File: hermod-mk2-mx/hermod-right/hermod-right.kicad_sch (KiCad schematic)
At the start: 45 parts, among them J1 USB_C_Receptacle_USB2.0, J2 Conn_01x05, J3 USB_C_Receptacle_USB2.0, Q3 MMUN2133LT1G, U1 STM32G474CETx, U2 PRTR5V0U2X, U3 XC6206PxxxMR-Regulator_Linear, U4 CR2013-MI2120, U5 PRTR5V0U2X, U8 SN74AHCT1G125DBVR

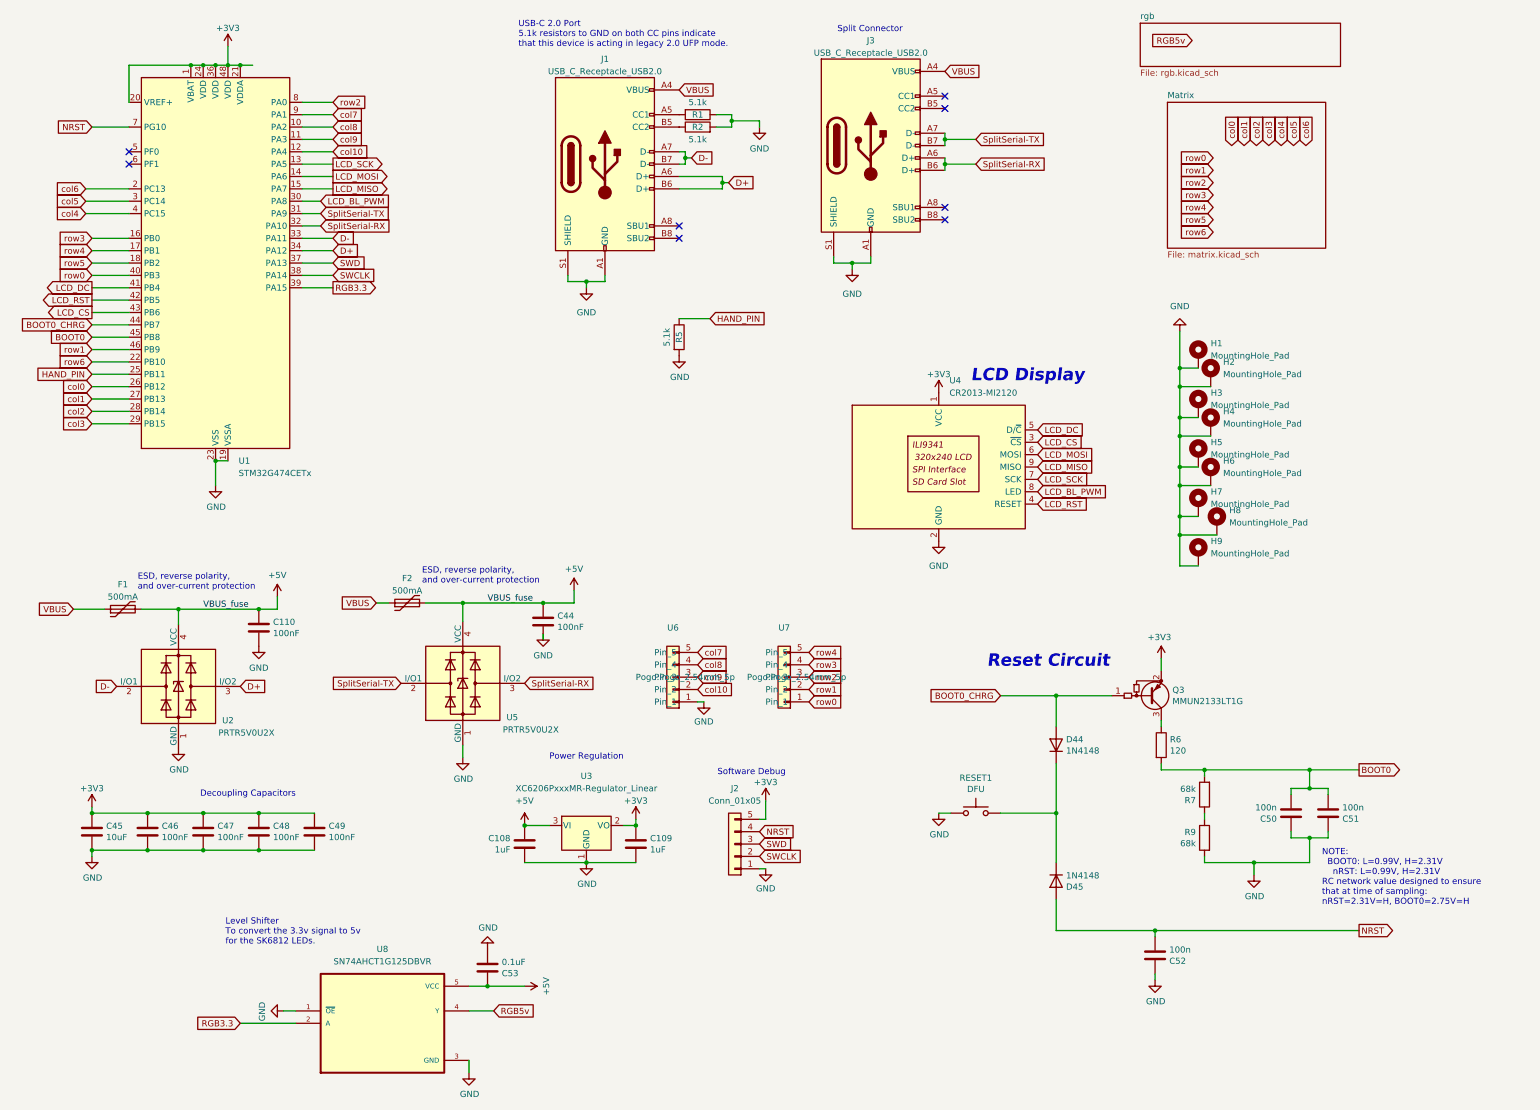
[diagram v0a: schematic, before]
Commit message: Added switches to hermod 3 and updated mist thumb spacing
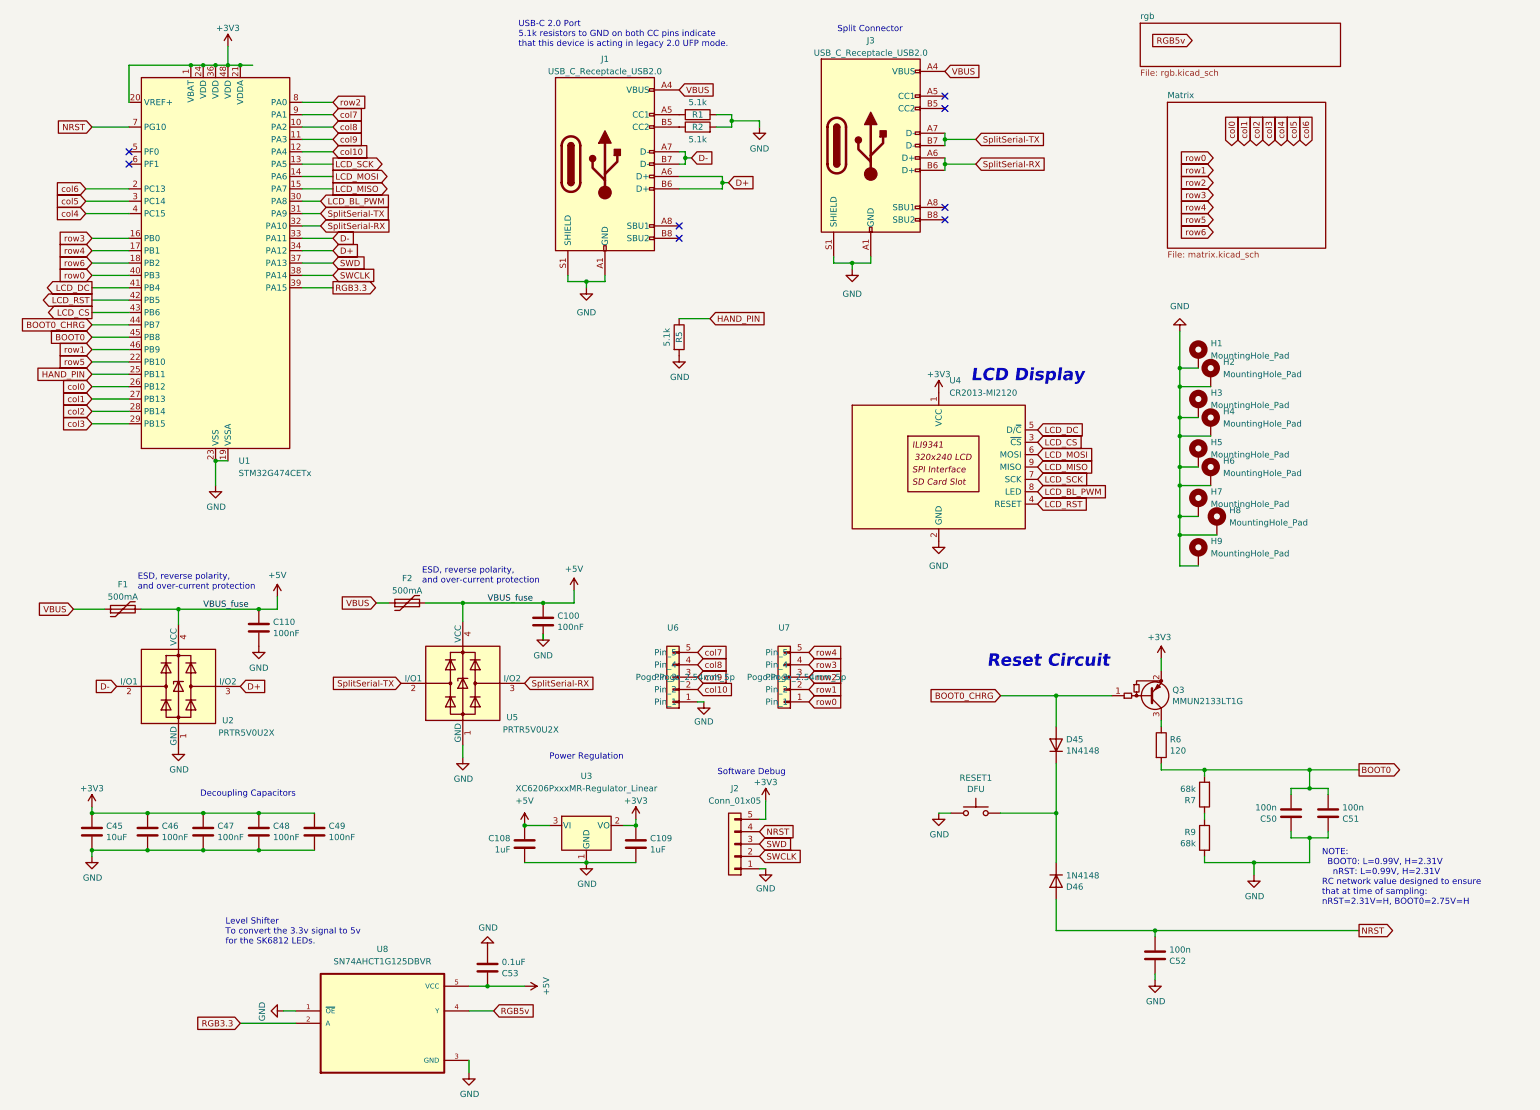
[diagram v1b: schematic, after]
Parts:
- renumbered C44 to C100, D44 to D45, D45 to D46
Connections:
- net row5: now also U1.22 (PB10); no longer U1.18 (PB2)
- net row6: now also U1.18 (PB2); no longer U1.22 (PB10)
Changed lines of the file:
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@@
 	(global_label "row6"
 		(shape input)
-		(at 25.4 85.09 180)
+		(at 25.4 64.77 180)
 		(fields_autoplaced yes)
 		(effects
@@
 		)
 		(property "Intersheetrefs" "${INTERSHEET_REFS}"
-			(at 17.9396 85.09 0)
+			(at 17.9396 64.77 0)
 			(effects
 				(font
@@
 	(global_label "row5"
 		(shape input)
-		(at 25.4 64.77 180)
+		(at 25.4 85.09 180)
 		(fields_autoplaced yes)
 		(effects
@@
 		)
 		(property "Intersheetrefs" "${INTERSHEET_REFS}"
-			(at 17.9396 64.77 0)
+			(at 17.9396 85.09 0)
 			(effects
 				(font
@@
 		(on_board yes)
 		(dnp no)
-		(property "Reference" "D44"
+		(property "Reference" "D45"
 			(at 225.552 162.6616 90)
 			(effects
@@
 			(project "hermod-right"
 				(path "/cb32b2da-a60d-4ed4-a57b-2c397f553171"
-					(reference "D44")
+					(reference "D45")
 					(unit 1)
 				)
@@
 		(on_board yes)
 		(dnp no)
-		(property "Reference" "D45"
+		(property "Reference" "D46"
 			(at 225.552 192.9384 90)
 			(effects
@@
 			(project "hermod-right"
 				(path "/cb32b2da-a60d-4ed4-a57b-2c397f553171"
-					(reference "D45")
+					(reference "D46")
 					(unit 1)
 				)
@@
 		(on_board yes)
 		(dnp no)
-		(property "Reference" "C44"
+		(property "Reference" "C100"
 			(at 121.031 137.2616 0)
 			(effects
@@
 			(project "hermod-right"
 				(path "/cb32b2da-a60d-4ed4-a57b-2c397f553171"
-					(reference "C44")
+					(reference "C100")
 					(unit 1)
 				)
